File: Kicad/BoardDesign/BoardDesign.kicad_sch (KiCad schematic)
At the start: 40 parts, among them IC1 HX717, IC2 RT9080-33GJ5, J1 Conn_01x04_Socket, J2 USB_C_Receptacle_USB2.0_16P, J3 Conn_01x04_Socket, J4 Conn_01x04_Socket, SW1 SW_SPST, SW2 SW_SPST, SW3 SW_SPST, SW4 SW_SPST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

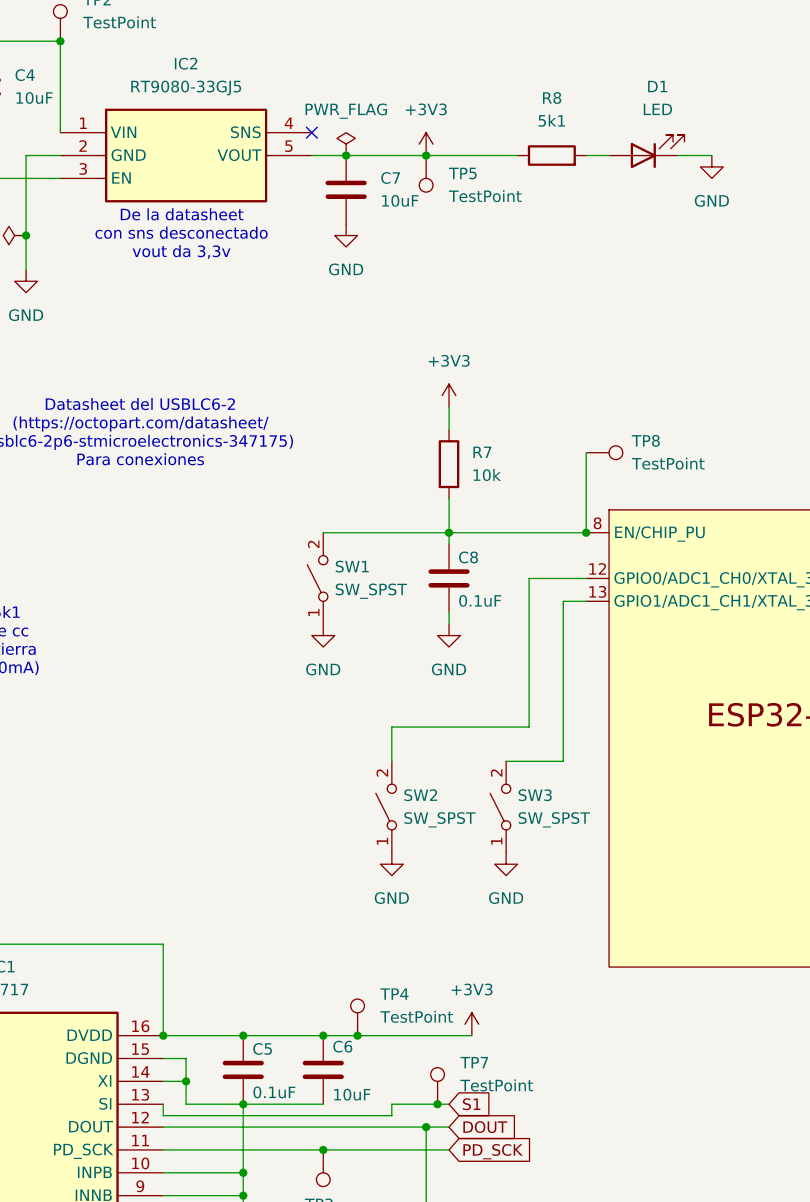
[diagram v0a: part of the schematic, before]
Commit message: Diseño placa semi terminado
Faltan un par de footprints
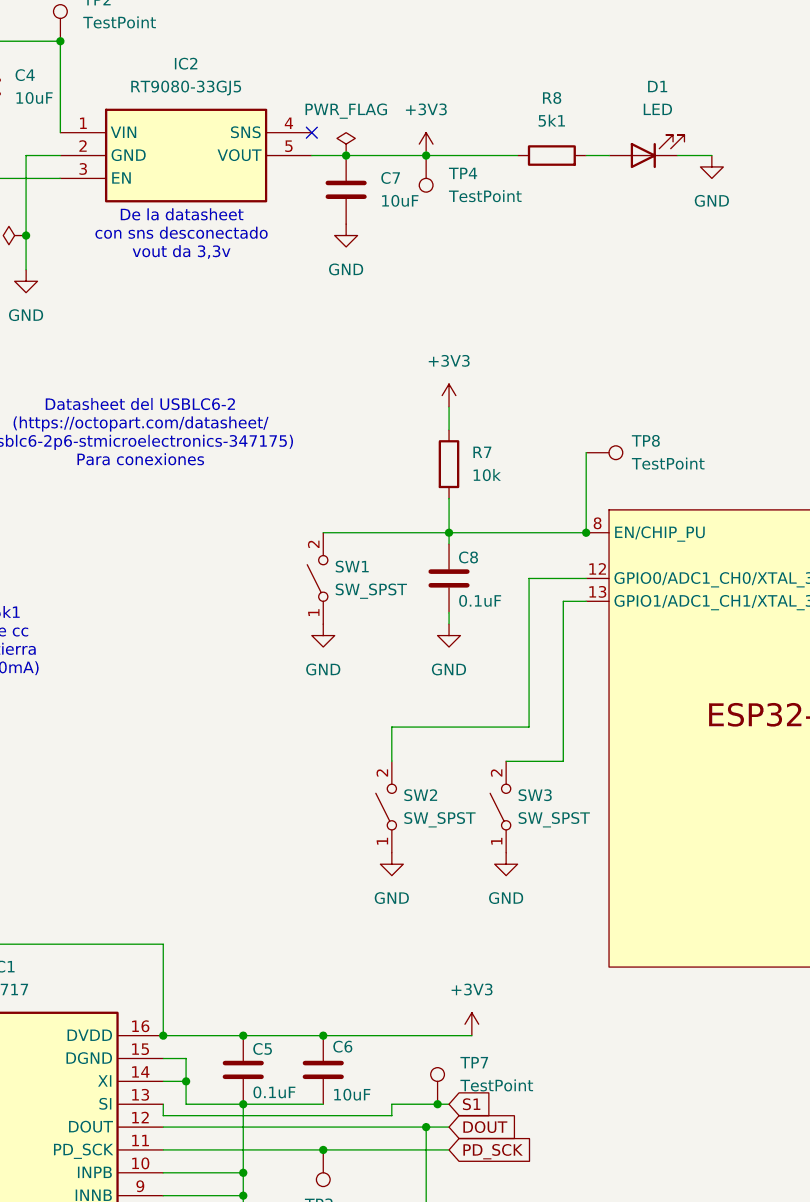
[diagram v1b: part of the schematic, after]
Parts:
- removed TP5: TestPoint, TestPoint:TestPoint_Pad_D1.5mm, symbol Connector:TestPoint
- C1, C3, C5, C8: JLCPCB (none) -> C14663
- C2, C4, C6, C7: JLCPCB (none) -> C19702
- IC1: JLCPCB (none) -> C575394
- IC2: JLCPCB (none) -> C2959864
- J1, J2, J3, J4: JLCPCB (none) -> C5116483
- R1, R10, R2, R5, R6, R7, R8, R9: footprint Capacitor_SMD:C_0603_1608Metric -> Resistor_SMD:R_0603_1608Metric; JLCPCB C4260 -> (none)
- R3, R4: footprint Capacitor_SMD:C_0603_1608Metric -> Resistor_SMD:R_0603_1608Metric; JLCPCB C166559 -> (none)
- TP1, TP2, TP3, TP4, TP6, TP7, TP8: footprint TestPoint:TestPoint_Pad_D1.5mm -> custom_footprints:TestPoint_Pad_D1.5mm_nosilk
- U1: JLCPCB (none) -> C2827693
- U2: JLCPCB (none) -> C2911374
